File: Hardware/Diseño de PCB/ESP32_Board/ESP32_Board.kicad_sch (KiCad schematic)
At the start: 8 parts, among them J1 Conn_02x15_Odd_Even, J2 Conn_01x02, J3 Conn_01x02, J4 Conn_01x05, U1 ESP32 - DEVKIT, U2 logo

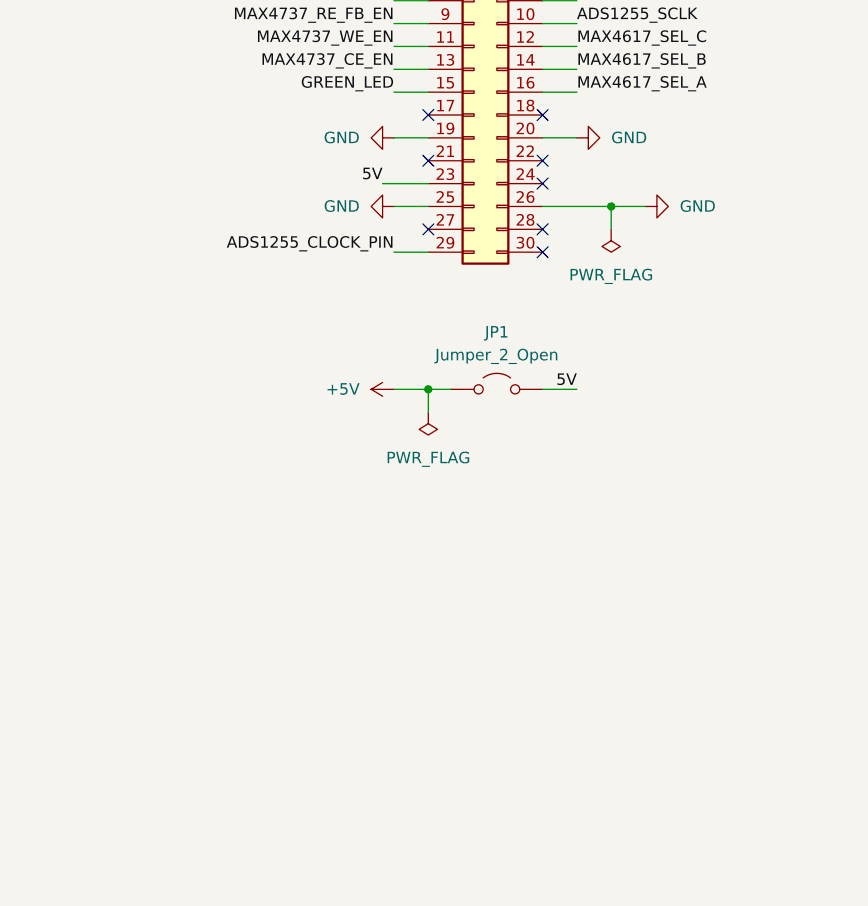
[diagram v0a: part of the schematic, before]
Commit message: Se resolvieron multiples incovenientes criticos en la interfaz y el backend. Principalmente, problemas que ralentizaban la lecturas de las muestras asociados con las graficas. Se agregaron tasas de refresco para los graficos para evitar actualizacion constante y saturación, sleep() al bucle del SerialWorker para evitar busy-wait al 100% y apertura y cierre unico de archivo de backup al principio y final del experimento (se estaba abriendo y cerrando por cada muestra leida). Además se resolvieron issues menores: método duplicado, np.asmatrix() deprecado, race condition en lectura de headers binarios, buffers O(n), import duplicado, path hardcodeado, autoRange que rompe el zoom manual, e inconsistencia LSV/CV en la nomenclatura.  Hardware: Se termino de diseñar la PCB de la ESP32, lista para fabricación. Firmware: small fixes.
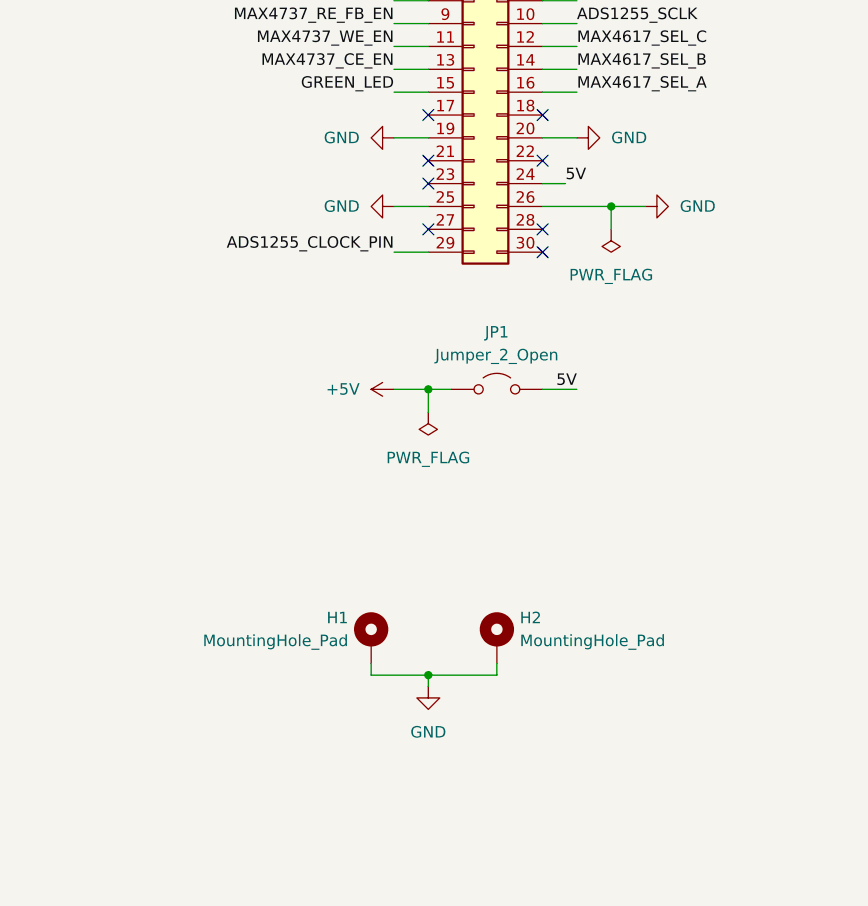
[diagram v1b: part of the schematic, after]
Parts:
- added H1, H2: MountingHole_Pad, MountingHole:MountingHole_2.2mm_M2_Pad_Via, symbol Mechanical:MountingHole_Pad
- J1: footprint Connector_PinHeader_2.54mm:PinHeader_2x16_P2.54mm_Horizontal -> Connector_PinHeader_2.54mm:PinHeader_2x15_P2.54mm_Horizontal
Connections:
- net 5V: now also J1.24 (Pin_24); no longer J1.23 (Pin_23)
- net GND: now also H1.1, H2.1

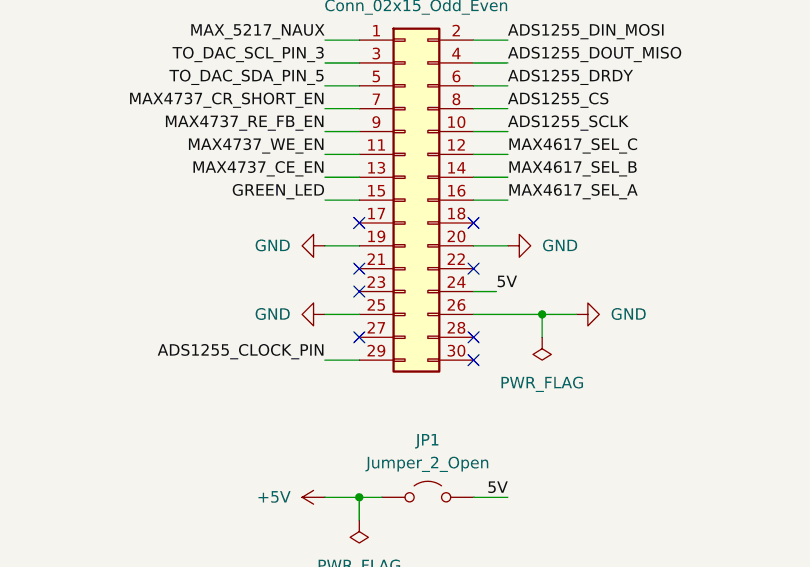
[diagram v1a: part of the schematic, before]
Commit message: ESP32 Board 5V pinout correction
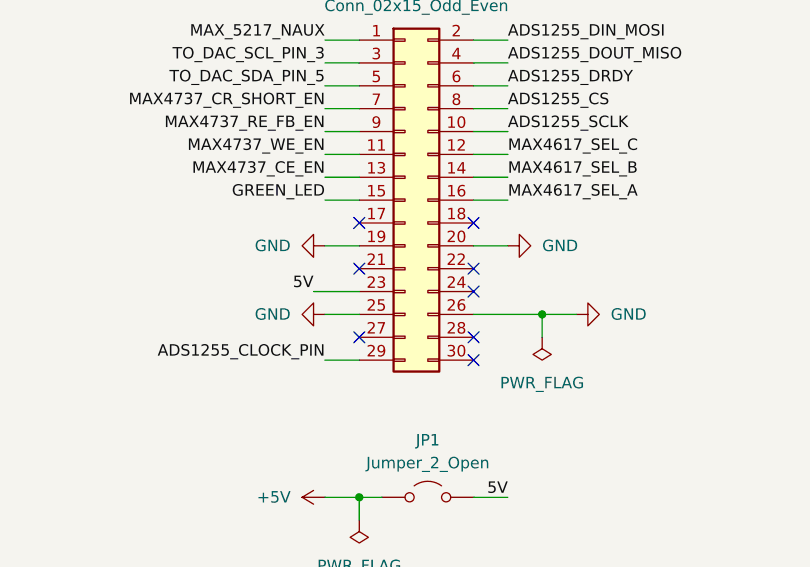
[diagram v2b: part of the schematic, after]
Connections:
- net 5V: now also J1.23 (Pin_23); no longer J1.24 (Pin_24)
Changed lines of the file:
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@@
 	)
 	(no_connect
-		(at 209.55 77.47)
+		(at 222.25 77.47)
 	)
 	(no_connect
@@
 	(wire
 		(pts
-			(xy 222.25 77.47) (xy 224.79 77.47)
-		)
-		(stroke
-			(width 0)
-			(type default)
-		)
-	)
-	(wire
-		(pts
 			(xy 222.25 64.77) (xy 226.06 64.77)
 		)
@@
 		(pts
 			(xy 229.87 80.01) (xy 233.68 80.01)
+		)
+		(stroke
+			(width 0)
+			(type default)
+		)
+	)
+	(wire
+		(pts
+			(xy 204.47 77.47) (xy 209.55 77.47)
 		)
 		(stroke
@@
 	)
 	(label "5V"
-		(at 224.79 77.47 0)
-		(fields_autoplaced yes)
-		(effects
-			(font
-				(size 1.27 1.27)
-			)
-			(justify left bottom)
-		)
-	)
+		(at 204.47 77.47 180)
+		(fields_autoplaced yes)
+		(effects
+			(font
+				(size 1.27 1.27)
+			)
+			(justify right bottom)
+		)
+	)
